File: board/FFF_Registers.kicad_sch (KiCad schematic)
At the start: 19 parts, among them U1 74F573, U14 74F32, U18 74F04, U2 74F541, U47 74F573, U48 74F541, U49 74F573, U50 74F541, U51 74F32, U52 74F04

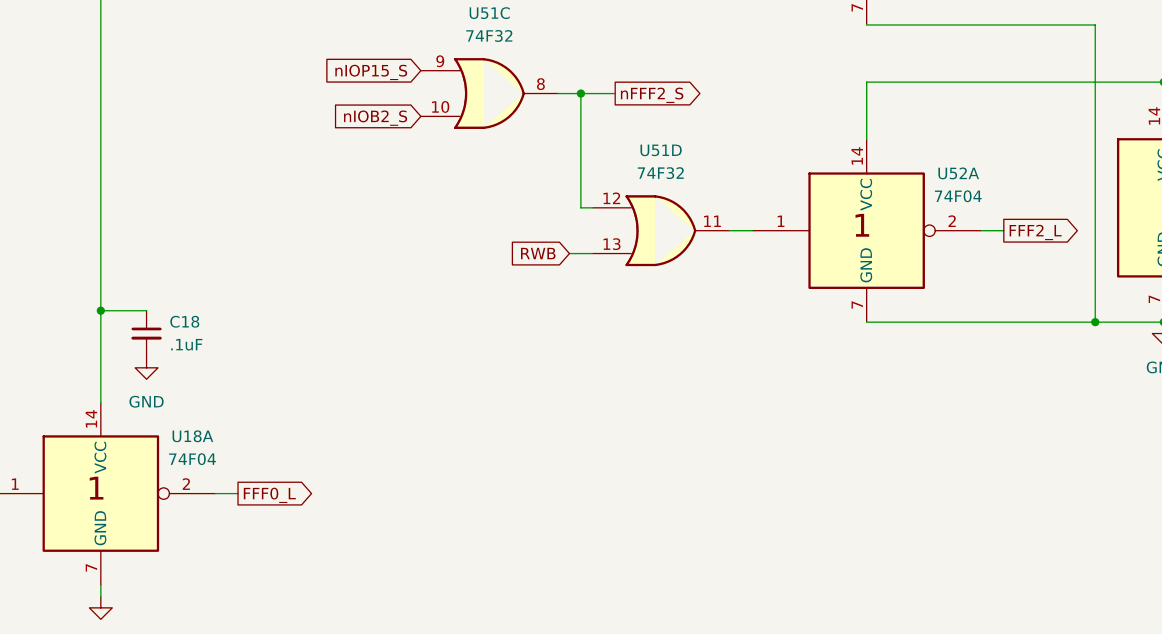
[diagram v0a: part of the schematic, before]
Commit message: Latest main PCB update with FFF1 and FFF2 added and decode logic updated to exclude FFFE and FFFF in nOSROM_S signal
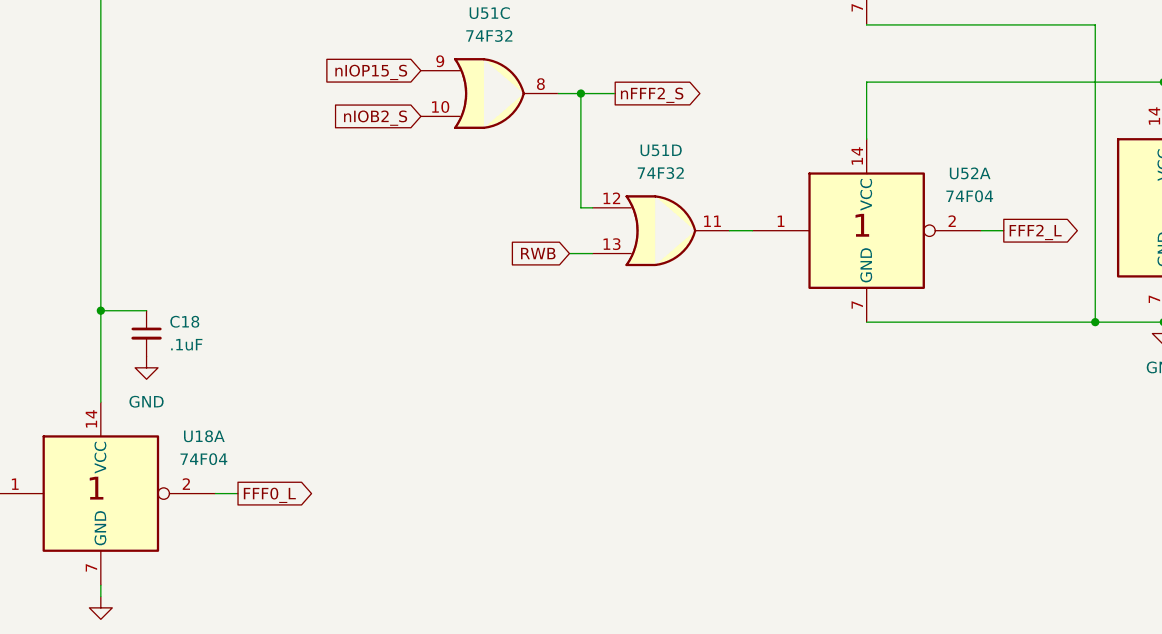
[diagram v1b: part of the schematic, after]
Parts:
- U1, U2, U47, U48, U49, U50: footprint Package_DIP:DIP-20_W7.62mm_LongPads -> Package_DIP:DIP-20_W7.62mm_Socket_LongPads
- U14, U18, U51, U52: footprint Package_DIP:DIP-14_W7.62mm_LongPads -> Package_DIP:DIP-14_W7.62mm_Socket_LongPads
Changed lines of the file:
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@@
 			)
 		)
-		(property "Footprint" "Package_DIP:DIP-14_W7.62mm_LongPads"
+		(property "Footprint" "Package_DIP:DIP-14_W7.62mm_Socket_LongPads"
 			(at 223.52 115.57 0)
 			(effects
@@
 			)
 		)
-		(property "Footprint" "Package_DIP:DIP-14_W7.62mm_LongPads"
+		(property "Footprint" "Package_DIP:DIP-14_W7.62mm_Socket_LongPads"
 			(at 115.57 177.8 0)
 			(effects
@@
 			)
 		)
-		(property "Footprint" "Package_DIP:DIP-14_W7.62mm_LongPads"
+		(property "Footprint" "Package_DIP:DIP-14_W7.62mm_Socket_LongPads"
 			(at 181.61 133.35 0)
 			(effects
@@
 			)
 		)
-		(property "Footprint" "Package_DIP:DIP-20_W7.62mm_LongPads"
+		(property "Footprint" "Package_DIP:DIP-20_W7.62mm_Socket_LongPads"
 			(at 156.21 54.61 0)
 			(effects
@@
 			)
 		)
-		(property "Footprint" "Package_DIP:DIP-14_W7.62mm_LongPads"
+		(property "Footprint" "Package_DIP:DIP-14_W7.62mm_Socket_LongPads"
 			(at 181.61 100.33 0)
 			(effects
@@
 			)
 		)
-		(property "Footprint" "Package_DIP:DIP-14_W7.62mm_LongPads"
+		(property "Footprint" "Package_DIP:DIP-14_W7.62mm_Socket_LongPads"
 			(at 256.54 146.05 0)
 			(effects
@@
 			)
 		)
-		(property "Footprint" "Package_DIP:DIP-14_W7.62mm_LongPads"
+		(property "Footprint" "Package_DIP:DIP-14_W7.62mm_Socket_LongPads"
 			(at 200.66 115.57 0)
 			(effects
@@
 			)
 		)
-		(property "Footprint" "Package_DIP:DIP-20_W7.62mm_LongPads"
+		(property "Footprint" "Package_DIP:DIP-20_W7.62mm_Socket_LongPads"
 			(at 102.87 54.61 0)
 			(effects
@@
 			)
 		)
-		(property "Footprint" "Package_DIP:DIP-20_W7.62mm_LongPads"
+		(property "Footprint" "Package_DIP:DIP-20_W7.62mm_Socket_LongPads"
 			(at 106.68 128.27 0)
 			(effects
@@
 			)
 		)
-		(property "Footprint" "Package_DIP:DIP-14_W7.62mm_LongPads"
+		(property "Footprint" "Package_DIP:DIP-14_W7.62mm_Socket_LongPads"
 			(at 200.66 148.59 0)
 			(effects
@@
 		(fields_autoplaced yes)
 		(property "Reference" "U18"
-			(at 148.59 171.4814 0)
+			(at 149.86 171.4814 0)
 			(effects
 				(font
@@
 		)
 		(property "Value" "74F04"
-			(at 148.59 174.0214 0)
-			(effects
-				(font
-					(size 1.27 1.27)
-				)
-			)
-		)
-		(property "Footprint" "Package_DIP:DIP-14_W7.62mm_LongPads"
+			(at 149.86 174.0214 0)
+			(effects
+				(font
+					(size 1.27 1.27)
+				)
+			)
+		)
+		(property "Footprint" "Package_DIP:DIP-14_W7.62mm_Socket_LongPads"
 			(at 138.43 177.8 0)
 			(effects
@@
 			)
 		)
-		(property "Footprint" "Package_DIP:DIP-14_W7.62mm_LongPads"
+		(property "Footprint" "Package_DIP:DIP-14_W7.62mm_Socket_LongPads"
 			(at 96.52 162.56 0)
 			(effects
@@
 			)
 		)
-		(property "Footprint" "Package_DIP:DIP-20_W7.62mm_LongPads"
+		(property "Footprint" "Package_DIP:DIP-20_W7.62mm_Socket_LongPads"
 			(at 60.96 128.27 0)
 			(effects
@@
 			)
 		)
-		(property "Footprint" "Package_DIP:DIP-20_W7.62mm_LongPads"
+		(property "Footprint" "Package_DIP:DIP-20_W7.62mm_Socket_LongPads"
 			(at 201.93 54.61 0)
 			(effects
@@
 		(fields_autoplaced yes)
 		(property "Reference" "U52"
-			(at 233.68 142.2714 0)
+			(at 234.95 142.2714 0)
 			(effects
 				(font
@@
 		)
 		(property "Value" "74F04"
-			(at 233.68 144.8114 0)
-			(effects
-				(font
-					(size 1.27 1.27)
-				)
-			)
-		)
-		(property "Footprint" "Package_DIP:DIP-14_W7.62mm_LongPads"
+			(at 234.95 144.8114 0)
+			(effects
+				(font
+					(size 1.27 1.27)
+				)
+			)
+		)
+		(property "Footprint" "Package_DIP:DIP-14_W7.62mm_Socket_LongPads"
 			(at 223.52 148.59 0)
 			(effects
@@
 			)
 		)
-		(property "Footprint" "Package_DIP:DIP-20_W7.62mm_LongPads"
+		(property "Footprint" "Package_DIP:DIP-20_W7.62mm_Socket_LongPads"
 			(at 57.15 54.61 0)
 			(effects

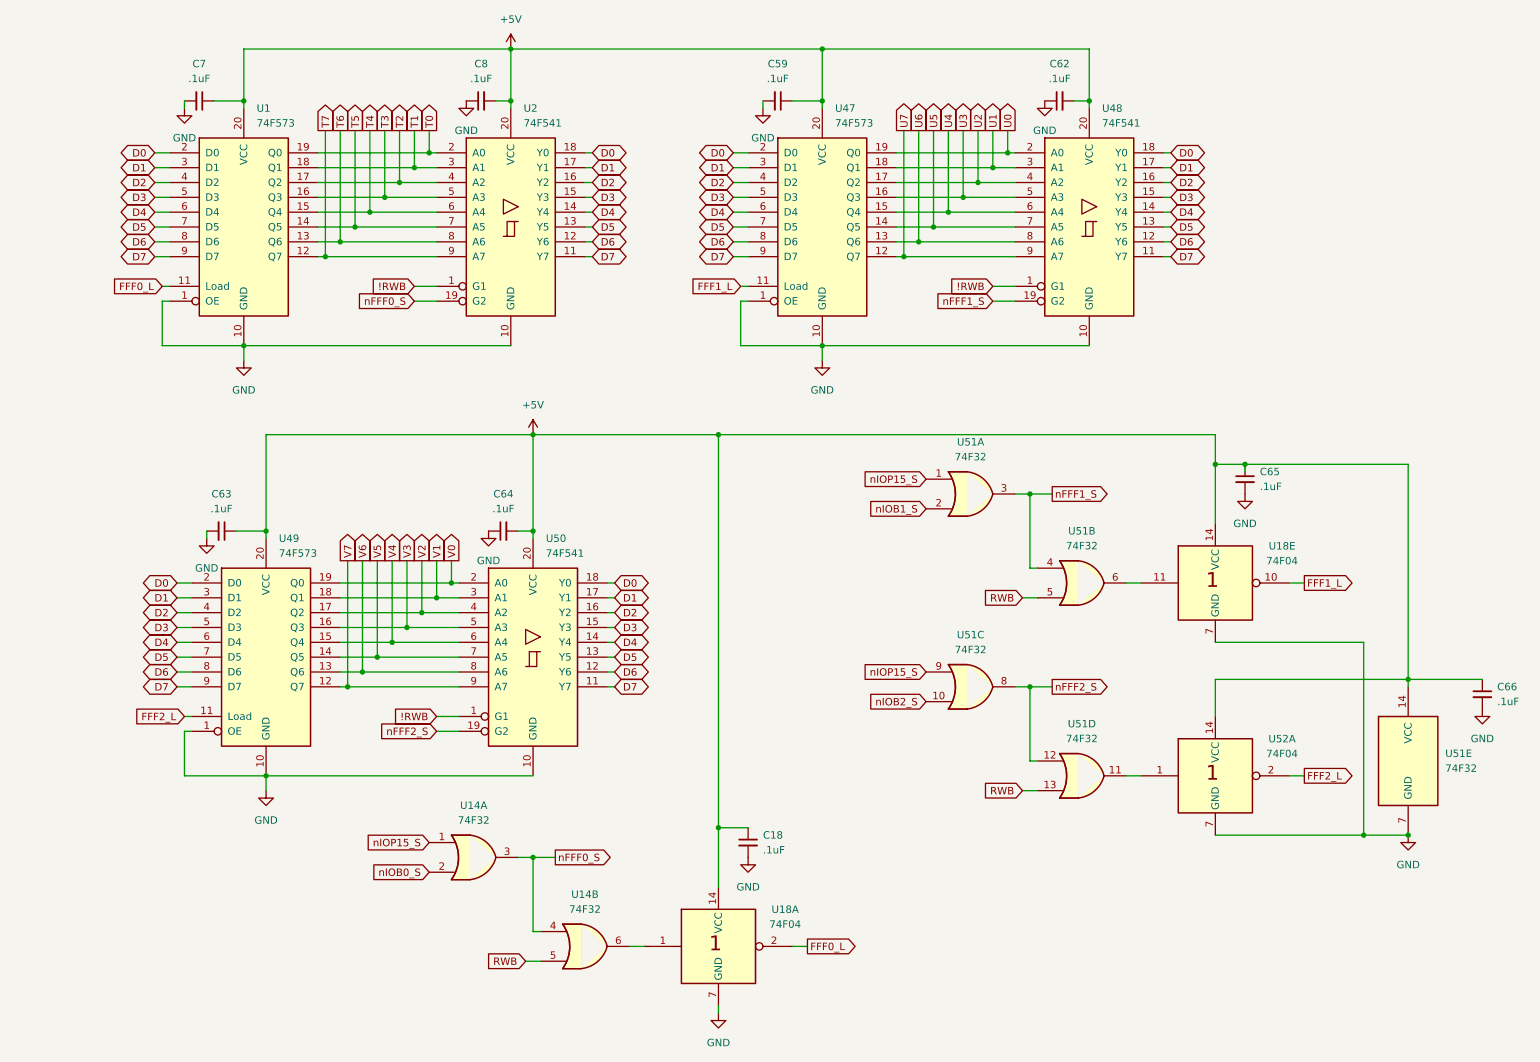
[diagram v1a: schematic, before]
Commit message: Schematic Bus updates, silkscreen updates, position tweaks, and other corrections.
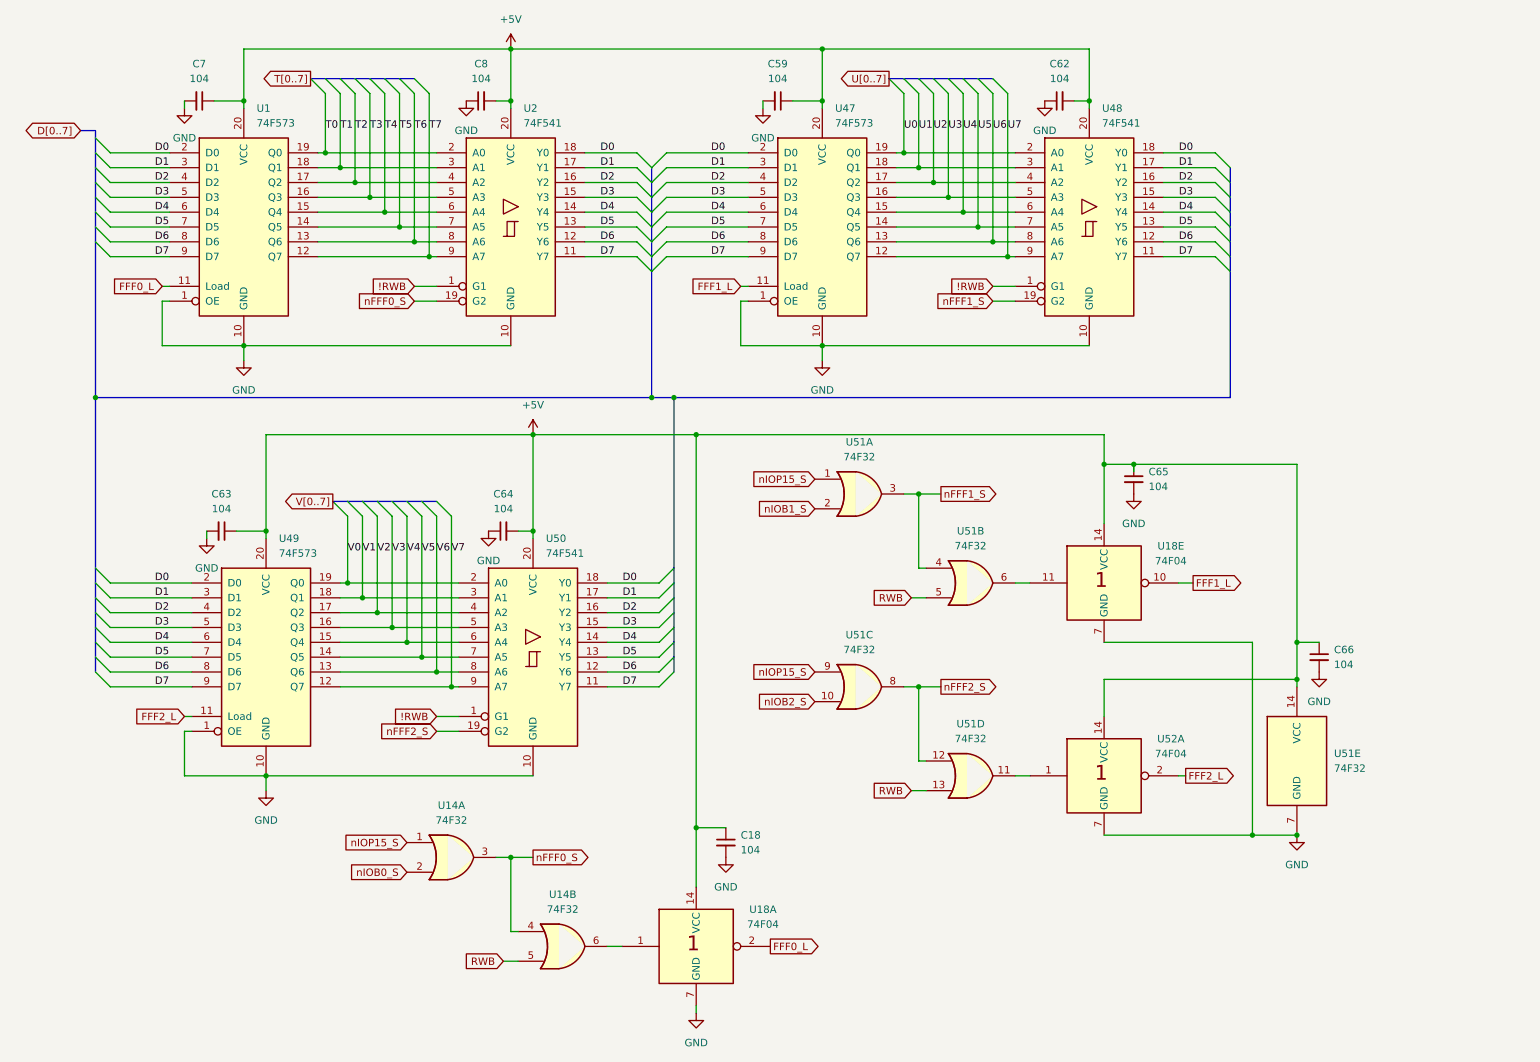
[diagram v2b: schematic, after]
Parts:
- C18, C59, C62, C63, C64, C65, C66, C7, C8: value .1uF -> 104
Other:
- company: (none) -> Data Tuning
- title: (none) -> FFFx Registers and Logic
- moved on the sheet: C18, C65, C66, U14A, U14B, U18A, U18E, U51A, U51B, U51C, U51D, U51E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
